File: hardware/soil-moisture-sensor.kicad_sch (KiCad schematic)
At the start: 34 parts, among them J1 USB_B_Micro, Q1 Q_NPN_BEC, Q2 Q_NPN_BEC, SW1 SW_Push, SW2 SW_Push, U2 CP2102N-Axx-xQFN24, U3 ESP32-WROOM-32D

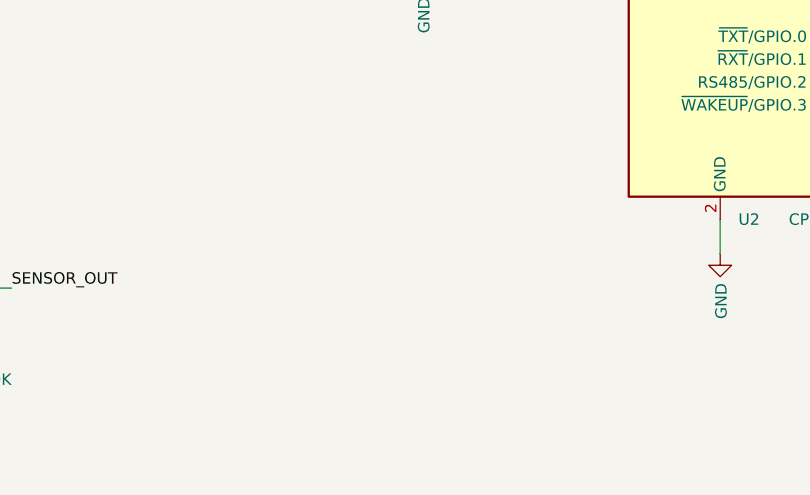
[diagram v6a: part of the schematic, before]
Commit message: added debug header and fixed more drc issues
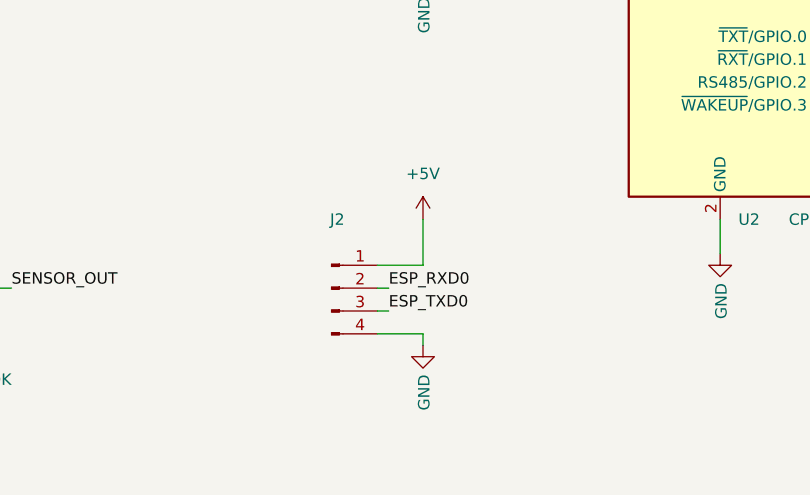
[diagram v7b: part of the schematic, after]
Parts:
- added J2: (no value), symbol Connector:Conn_01x04_Male
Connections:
- net +5V: now also J2.1 (Pin_1)
- net ESP_RXD0: now also J2.2 (Pin_2)
- net ESP_TXD0: now also J2.3 (Pin_3)
- net GND: now also J2.4 (Pin_4)
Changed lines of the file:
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@@
+    (stroke (width 0) (type default) (color 0 0 0 0))
+  )
+  (wire (pts (xy 134.62 175.26) (xy 129.54 175.26))
     (stroke (width 0) (type default) (color 0 0 0 0))
   )
@@
     (stroke (width 0) (type default) (color 0 0 0 0))
   )
+  (wire (pts (xy 129.54 172.72) (xy 130.81 172.72))
+    (stroke (width 0) (type default) (color 0 0 0 0))
+  )
   (wire (pts (xy 196.85 142.24) (xy 196.85 144.78))
     (stroke (width 0) (type default) (color 0 0 0 0))
   )
+  (wire (pts (xy 134.62 162.56) (xy 134.62 167.64))
+    (stroke (width 0) (type default) (color 0 0 0 0))
+  )
   (wire (pts (xy 190.5 22.86) (xy 196.85 22.86))
     (stroke (width 0) (type default) (color 0 0 0 0))
@@
     (stroke (width 0) (type default) (color 0 0 0 0))
   )
+  (wire (pts (xy 129.54 170.18) (xy 130.81 170.18))
+    (stroke (width 0) (type default) (color 0 0 0 0))
+  )
   (wire (pts (xy 214.63 144.78) (xy 222.25 144.78))
     (stroke (width 0) (type default) (color 0 0 0 0))
@@
     (stroke (width 0) (type default) (color 0 0 0 0))
   )
+  (wire (pts (xy 134.62 176.53) (xy 134.62 175.26))
+    (stroke (width 0) (type default) (color 0 0 0 0))
+  )
   (wire (pts (xy 172.72 53.34) (xy 172.72 55.88))
     (stroke (width 0) (type default) (color 0 0 0 0))
@@
   )
   (wire (pts (xy 30.48 135.89) (xy 53.34 135.89))
+    (stroke (width 0) (type default) (color 0 0 0 0))
+  )
+  (wire (pts (xy 134.62 167.64) (xy 129.54 167.64))
     (stroke (width 0) (type default) (color 0 0 0 0))
   )
@@
     (effects (font (size 1.27 1.27)) (justify left bottom))
   )
+  (label "ESP_TXD0" (at 130.81 172.72 0)
+    (effects (font (size 1.27 1.27)) (justify left bottom))
+  )
   (label "IO23" (at 259.08 107.95 0)
+    (effects (font (size 1.27 1.27)) (justify left bottom))
+  )
+  (label "ESP_RXD0" (at 130.81 170.18 0)
     (effects (font (size 1.27 1.27)) (justify left bottom))
   )
@@
     (pin "2")
   )
+  (symbol (lib_id "power:GND") (at 134.62 176.53 0) (unit 1)
+    (in_bom yes) (on_board yes)
+    (property "Reference" "#PWR02" (id 0) (at 134.62 182.88 0)
+      (effects (font (size 1.27 1.27)) hide)
+    )
+    (property "Value" "GND" (id 1) (at 134.747 179.7812 90)
+      (effects (font (size 1.27 1.27)) (justify right))
+    )
+    (property "Footprint" "" (id 2) (at 134.62 176.53 0)
+      (effects (font (size 1.27 1.27)) hide)
+    )
+    (property "Datasheet" "" (id 3) (at 134.62 176.53 0)
+      (effects (font (size 1.27 1.27)) hide)
+    )
+    (pin "1")
+  )
   (symbol (lib_id "Device:C") (at 196.85 26.67 0) (unit 1)
     (in_bom yes) (on_board yes)
@@
     (pin "1")
     (pin "2")
+  )
+  (symbol (lib_id "power:+5V") (at 134.62 162.56 0) (unit 1)
+    (in_bom yes) (on_board yes) (fields_autoplaced)
+    (property "Reference" "#PWR01" (id 0) (at 134.62 166.37 0)
+      (effects (font (size 1.27 1.27)) hide)
+    )
+    (property "Value" "+5V" (id 1) (at 134.62 157.48 0))
+    (property "Footprint" "" (id 2) (at 134.62 162.56 0)
+      (effects (font (size 1.27 1.27)) hide)
+    )
+    (property "Datasheet" "" (id 3) (at 134.62 162.56 0)
+      (effects (font (size 1.27 1.27)) hide)
+    )
+    (pin "1")
   )
   (symbol (lib_id "power:+5V") (at 165.1 100.33 0) (unit 1)
@@
     (pin "2")
   )
+  (symbol (lib_id "Connector:Conn_01x04_Male") (at 124.46 170.18 0) (unit 1)
+    (in_bom yes) (on_board yes) (fields_autoplaced)
+    (property "Reference" "J2" (id 0) (at 125.095 162.56 0))
+    (property "Value" "" (id 1) (at 125.095 165.1 0))
+    (property "Footprint" "" (id 2) (at 124.46 170.18 0)
+      (effects (font (size 1.27 1.27)) hide)
+    )
+    (property "Datasheet" "~" (id 3) (at 124.46 170.18 0)
+      (effects (font (size 1.27 1.27)) hide)
+    )
+    (pin "1")
+    (pin "2")
+    (pin "3")
+    (pin "4")
+  )
   (symbol (lib_id "Device:C") (at 107.95 54.61 90) (unit 1)
     (in_bom yes) (on_board yes)
@@
   )
   (symbol_instances
+    (path "/a58cb8c9-d51f-4422-9c66-8f34ef5ca3fa"
+      (reference "#PWR01") (unit 1) (value "+5V") (footprint "")
+    )
+    (path "/84701d48-6155-43de-9641-a7906b4c20d9"
+      (reference "#PWR02") (unit 1) (value "GND") (footprint "")
+    )
     (path "/00000000-0000-0000-0000-00005f40b3ac"
       (reference "#PWR0101") (unit 1) (value "+BATT") (footprint "")
@@
       (reference "J1") (unit 1) (value "USB_B_Micro") (footprint "Connector_USB:USB_Micro-B_Molex_47346-0001")
     )
+    (path "/e73ba54f-b826-40a9-83b5-80a32ffbf61c"
+      (reference "J2") (unit 1) (value "Conn_01x04_Male") (footprint "Connector_PinSocket_2.54mm:PinSocket_1x04_P2.54mm_Vertical")
+    )
     (path "/c64813dc-7d54-43e7-ad5d-f020292deff3"

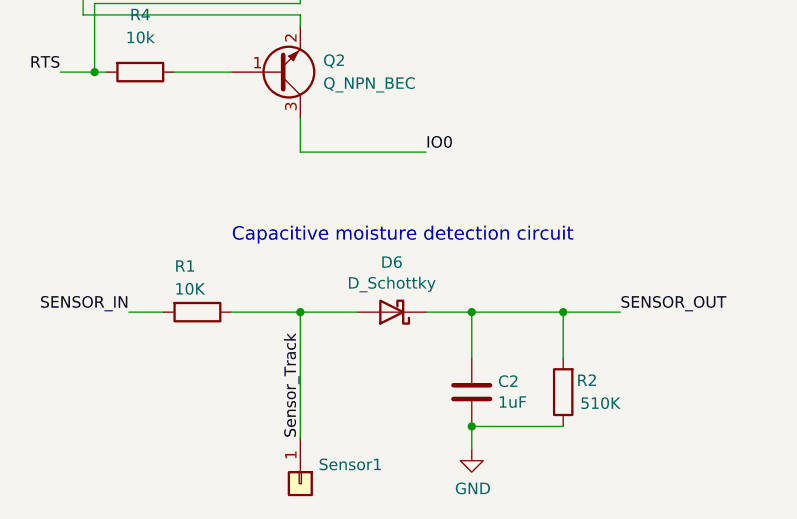
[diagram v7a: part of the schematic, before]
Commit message: changed diode to one in stock on lcsc
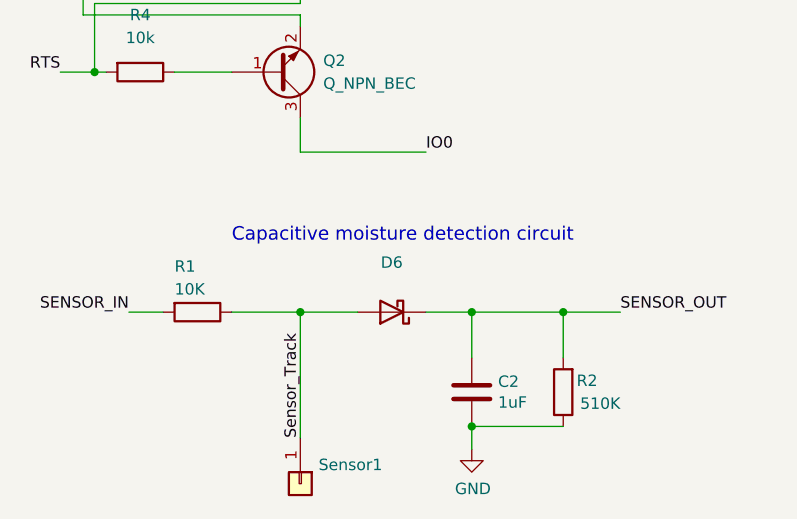
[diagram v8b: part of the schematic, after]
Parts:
- D6: value D_Schottky -> (none); footprint Diode_SMD:D_SOD-323_HandSoldering -> (none); LCSC C154819 -> C12744
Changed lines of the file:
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@@
     (in_bom yes) (on_board yes)
     (property "Reference" "D6" (id 0) (at 63.5 164.6682 0))
-    (property "Value" "D_Schottky" (id 1) (at 63.5 166.9796 0))
-    (property "Footprint" "Diode_SMD:D_SOD-323_HandSoldering" (id 2) (at 63.5 170.18 0)
+    (property "Value" "" (id 1) (at 63.5 166.9796 0))
+    (property "Footprint" "" (id 2) (at 63.5 170.18 0)
       (effects (font (size 1.27 1.27)) hide)
     )
@@
       (effects (font (size 1.27 1.27)) hide)
     )
-    (property "LCSC" "C154819" (id 4) (at 63.5 170.18 0)
+    (property "LCSC" "C12744" (id 4) (at 63.5 170.18 0)
       (effects (font (size 1.27 1.27)) hide)
     )
